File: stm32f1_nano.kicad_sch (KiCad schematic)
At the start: 49 parts, among them J1 Analog, J2 Digital, J3 TYPE-C-31-M-12, J5 DEBUG, Q1 AO3401A, U1 STM32F103C8T6, U2 W25Q128JVSIQ, U3 AMS1117-3.3, U4 XC6206P332MR, U5 AMS1117-5.0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

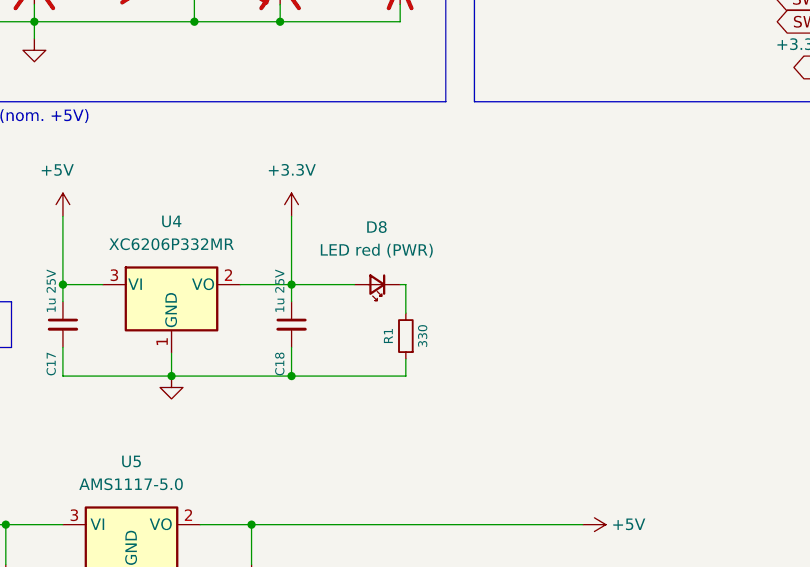
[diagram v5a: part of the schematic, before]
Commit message: #8 Use green power led
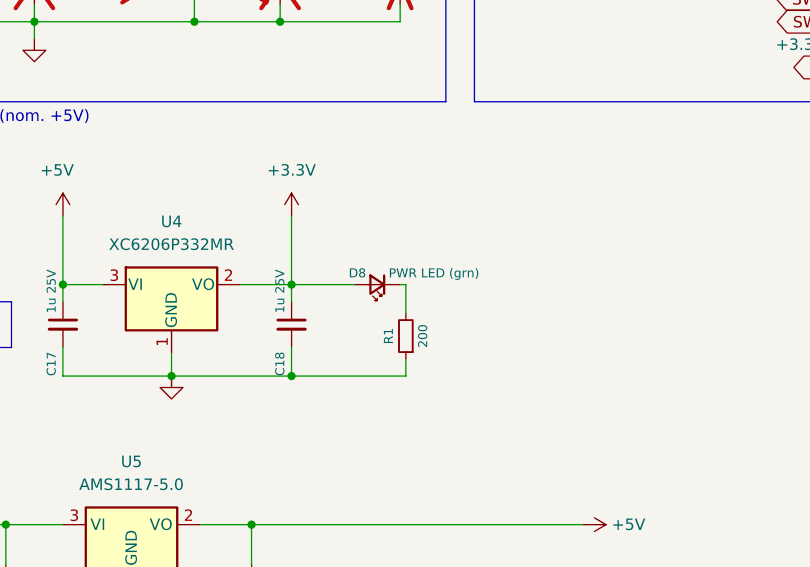
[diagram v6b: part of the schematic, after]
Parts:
- D8: value LED red (PWR) -> PWR LED (grn); JLCPCB Part # C2286 -> C72043; Manufacturer Hubei KENTO Elec -> Everlight Elec; Manufacturer_Name Hubei KENTO Elec -> Everlight Elec; Manufacturer_Part_Number KT-0603R -> 19-217/GHC-YR1S2/3T; Partnumber KT-0603R -> 19-217/GHC-YR1S2/3T
- R1: value 330 -> 200; JLCPCB Part # C25104 -> C25087; Partnumber 0402WGF3300TCE -> 0402WGF2000TCE
- U4: footprint Package_TO_SOT_SMD:SOT-23-3 -> Package_TO_SOT_SMD:SOT-23
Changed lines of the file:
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@@
     )
   )
-  (symbol (lib_id "Device:R_Small") (at 82.55 153.035 180) (unit 1)
-    (in_bom yes) (on_board yes) (dnp no)
-    (property "Reference" "R1" (at 80.645 153.035 90)
-      (effects (font (size 1 1)))
-    )
-    (property "Value" "330" (at 84.455 153.035 90)
-      (effects (font (size 1 1)))
-    )
-    (property "Footprint" "Resistor_SMD:R_0402_1005Metric" (at 82.55 153.035 0)
-      (effects (font (size 1.27 1.27)) hide)
-    )
-    (property "Datasheet" "~" (at 82.55 153.035 0)
-      (effects (font (size 1.27 1.27)) hide)
-    )
-    (property "Description" "62.5mW Thick Film Resistors ±100ppm/℃ ±1% 330Ω 0402  Chip Resistor - Surface Mount ROHS" (at 82.55 153.035 0)
-      (effects (font (size 1.27 1.27)) hide)
-    )
-    (property "JLCPCB Part #" "C25104" (at 82.55 153.035 0)
-      (effects (font (size 1.27 1.27)) hide)
-    )
-    (property "Manufacturer" "UNI-ROYAL(Uniroyal Elec)" (at 82.55 153.035 0)
-      (effects (font (size 1.27 1.27)) hide)
-    )
-    (property "Partnumber" "0402WGF3300TCE" (at 82.55 153.035 0)
-      (effects (font (size 1.27 1.27)) hide)
-    )
-    (property "isBasicPart" "YES" (at 82.55 153.035 0)
-      (effects (font (size 1.27 1.27)) hide)
-    )
-    (pin "1")
-    (pin "2")
-    (instances
-      (project "stm32f1_nano"
-        (path "/0d35483a-0b12-46cc-b9f2-896fd6831779"
-          (reference "R1") (unit 1)
-        )
-      )
-      (project "stm32f407vg"
-        (path "/2d452db2-a0cd-4a57-9497-df1dd0591a30"
-          (reference "R123") (unit 1)
-        )
-        (path "/2d452db2-a0cd-4a57-9497-df1dd0591a30/cb9cd892-4fab-4f54-9695-d8ba54556bb0"
-          (reference "R252") (unit 1)
-        )
-        (path "/2d452db2-a0cd-4a57-9497-df1dd0591a30/480569e0-5dbc-4314-a9d6-1dbd834f5833"
-          (reference "R502") (unit 1)
-        )
-        (path "/2d452db2-a0cd-4a57-9497-df1dd0591a30/3fc0c7b9-3f68-401d-a562-a4bf607ef36a"
-          (reference "R301") (unit 1)
-        )
-      )
-      (project "basicparts"
-        (path "/43a31acf-2604-4bbd-9556-e633c3dff6c4"
-          (reference "R114") (unit 1)
-        )
-      )
-    )
-  )
   (symbol (lib_id "power:+12V") (at 29.845 62.23 90) (unit 1)
     (in_bom yes) (on_board yes) (dnp no)
@@
     )
   )
+  (symbol (lib_id "Device:LED_Small") (at 79.375 147.32 180) (unit 1)
+    (in_bom yes) (on_board yes) (dnp no)
+    (property "Reference" "D8" (at 76.2 146.05 0)
+      (effects (font (size 1 1)) (justify right))
+    )
+    (property "Value" "PWR LED (grn)" (at 80.645 146.05 0)
+      (effects (font (size 1 1)) (justify right))
+    )
+    (property "Footprint" "LED_SMD:LED_0603_1608Metric" (at 79.375 147.32 90)
+      (effects (font (size 1 1)) hide)
+    )
+    (property "Datasheet" "https://datasheet.lcsc.com/lcsc/1811101510_Everlight-Elec-19-217-GHC-YR1S2-3T_C72043.pdf" (at 79.375 147.32 90)
+      (effects (font (size 1 1)) hide)
+    )
+    (property "Description" "Colorless transparence -40℃~+85℃ 520nm~535nm Emerald 120° 110mW 0603  Light Emitting Diodes (LED) ROHS" (at 79.375 147.32 0)
+      (effects (font (size 1 1)) hide)
+    )
+    (property "Manufacturer" "Everlight Elec" (at 79.375 147.32 0)
+      (effects (font (size 1 1)) hide)
+    )
+    (property "Partnumber" "19-217/GHC-YR1S2/3T" (at 79.375 147.32 0)
+      (effects (font (size 1 1)) hide)
+    )
+    (property "JLCPCB Part #" "C72043" (at 79.375 147.32 0)
+      (effects (font (size 1 1)) hide)
+    )
+    (property "Manufacturer_Name" "Everlight Elec" (at 79.375 147.32 0)
+      (effects (font (size 1 1)) hide)
+    )
+    (property "Manufacturer_Part_Number" "19-217/GHC-YR1S2/3T" (at 79.375 147.32 0)
+      (effects (font (size 1 1)) hide)
+    )
+    (property "isBasicPart" "YES" (at 79.375 147.32 0)
+      (effects (font (size 1 1)) hide)
+    )
+    (pin "1")
+    (pin "2")
+    (instances
+      (project "stm32f1_nano"
+        (path "/0d35483a-0b12-46cc-b9f2-896fd6831779"
+          (reference "D8") (unit 1)
+        )
+      )
+      (project "stm32f407vg"
+        (path "/2d452db2-a0cd-4a57-9497-df1dd0591a30"
+          (reference "D1") (unit 1)
+        )
+        (path "/2d452db2-a0cd-4a57-9497-df1dd0591a30/3fc0c7b9-3f68-401d-a562-a4bf607ef36a"
+          (reference "D301") (unit 1)
+        )
+      )
+      (project "basicparts"
+        (path "/43a31acf-2604-4bbd-9556-e633c3dff6c4"
+          (reference "D3") (unit 1)
+        )
+      )
+    )
+  )
   (symbol (lib_id "Regulator_Linear:AMS1117-3.3") (at 59.055 107.95 0) (unit 1)
     (in_bom no) (on_board no) (dnp yes) (fields_autoplaced)
@@
       (effects (font (size 1.27 1.27)))
     )
-    (property "Footprint" "Package_TO_SOT_SMD:SOT-23-3" (at 56.515 141.605 0)
+    (property "Footprint" "Package_TO_SOT_SMD:SOT-23" (at 56.515 141.605 0)
       (effects (font (size 1.27 1.27) italic) hide)
     )
@@
     )
   )
+  (symbol (lib_id "Device:R_Small") (at 82.55 153.035 180) (unit 1)
+    (in_bom yes) (on_board yes) (dnp no)
+    (property "Reference" "R1" (at 80.645 153.035 90)
+      (effects (font (size 1 1)))
+    )
+    (property "Value" "200" (at 84.455 153.035 90)
+      (effects (font (size 1 1)))
+    )
+    (property "Footprint" "Resistor_SMD:R_0402_1005Metric" (at 82.55 153.035 0)
+      (effects (font (size 1 1)) hide)
+    )
+    (property "Datasheet" "~" (at 82.55 153.035 0)
+      (effects (font (size 1 1)) hide)
+    )
+    (property "Description" "62.5mW Thick Film Resistors ±100ppm/℃ ±1% 200Ω 0402  Chip Resistor - Surface Mount ROHS" (at 82.55 153.035 0)
+      (effects (font (size 1 1)) hide)
+    )
+    (property "JLCPCB Part #" "C25087" (at 82.55 153.035 0)
+      (effects (font (size 1 1)) hide)
+    )
+    (property "Manufacturer" "UNI-ROYAL(Uniroyal Elec)" (at 82.55 153.035 0)
+      (effects (font (size 1 1)) hide)
+    )
+    (property "Partnumber" "0402WGF2000TCE" (at 82.55 153.035 0)
+      (effects (font (size 1 1)) hide)
+    )
+    (property "isBasicPart" "YES" (at 82.55 153.035 0)
+      (effects (font (size 1 1)) hide)
+    )
+    (pin "1")
+    (pin "2")
+    (instances
+      (project "stm32f1_nano"
+        (path "/0d35483a-0b12-46cc-b9f2-896fd6831779"
+          (reference "R1") (unit 1)
+        )
+      )
+      (project "stm32f407vg"
+        (path "/2d452db2-a0cd-4a57-9497-df1dd0591a30"
+          (reference "R123") (unit 1)
+        )
+        (path "/2d452db2-a0cd-4a57-9497-df1dd0591a30/cb9cd892-4fab-4f54-9695-d8ba54556bb0"
+          (reference "R252") (unit 1)
+        )
+        (path "/2d452db2-a0cd-4a57-9497-df1dd0591a30/480569e0-5dbc-4314-a9d6-1dbd834f5833"
+          (reference "R503") (unit 1)
+        )
+      )
+      (project "basicparts"
+        (path "/43a31acf-2604-4bbd-9556-e633c3dff6c4"
+          (reference "R8") (unit 1)
+        )
+      )
+    )
+  )
   (symbol (lib_id "Device:R_Small") (at 81.915 113.665 180) (unit 1)
     (in_bom no) (on_board no) (dnp yes)
@@
         )
       )
-    )
-  )
-  (symbol (lib_id "Device:LED_Small") (at 79.375 147.32 180) (unit 1)
-    (in_bom yes) (on_board yes) (dnp no) (fields_autoplaced)
-    (property "Reference" "D8" (at 79.3115 140.97 0)
-      (effects (font (size 1.27 1.27)))
-    )
-    (property "Value" "LED red (PWR)" (at 79.3115 143.51 0)
-      (effects (font (size 1.27 1.27)))
-    )
-    (property "Footprint" "LED_SMD:LED_0603_1608Metric" (at 79.375 147.32 90)
-      (effects (font (size 1.27 1.27)) hide)
-    )
-    (property "Datasheet" "~" (at 79.375 147.32 90)
-      (effects (font (size 1.27 1.27)) hide)
-    )
-    (property "Description" "-40℃~+85℃ Red 0603  Light Emitting Diodes (LED) ROHS" (at 79.375 147.32 0)
-      (effects (font (size 1.27 1.27)) hide)
-    )
-    (property "Manufacturer" "Hubei KENTO Elec" (at 79.375 147.32 0)
-      (effects (font (size 1.27 1.27)) hide)
-    )
-    (property "Partnumber" "KT-0603R" (at 79.375 147.32 0)
-      (effects (font (size 1.27 1.27)) hide)
-    )
-    (property "JLCPCB Part #" "C2286" (at 79.375 147.32 0)
-      (effects (font (size 1.27 1.27)) hide)
-    )
-    (property "Manufacturer_Name" "Hubei KENTO Elec" (at 79.375 147.32 0)
-      (effects (font (size 1.27 1.27)) hide)
-    )
-    (property "Manufacturer_Part_Number" "KT-0603R" (at 79.375 147.32 0)
-      (effects (font (size 1.27 1.27)) hide)
-    )
-    (property "isBasicPart" "YES" (at 79.375 147.32 0)
-      (effects (font (size 1.27 1.27)) hide)
-    )
-    (pin "1")
-    (pin "2")
-    (instances
-      (project "stm32f1_nano"
-        (path "/0d35483a-0b12-46cc-b9f2-896fd6831779"
-          (reference "D8") (unit 1)
-        )
-      )
-      (project "stm32f407vg"
-        (path "/2d452db2-a0cd-4a57-9497-df1dd0591a30"
-          (reference "D1") (unit 1)
-        )
-        (path "/2d452db2-a0cd-4a57-9497-df1dd0591a30/3fc0c7b9-3f68-401d-a562-a4bf607ef36a"
-          (reference "D301") (unit 1)
-        )
-      )
-      (project "basicparts"
-        (path "/43a31acf-2604-4bbd-9556-e633c3dff6c4"
-          (reference "D105") (unit 1)
-        )
-      )

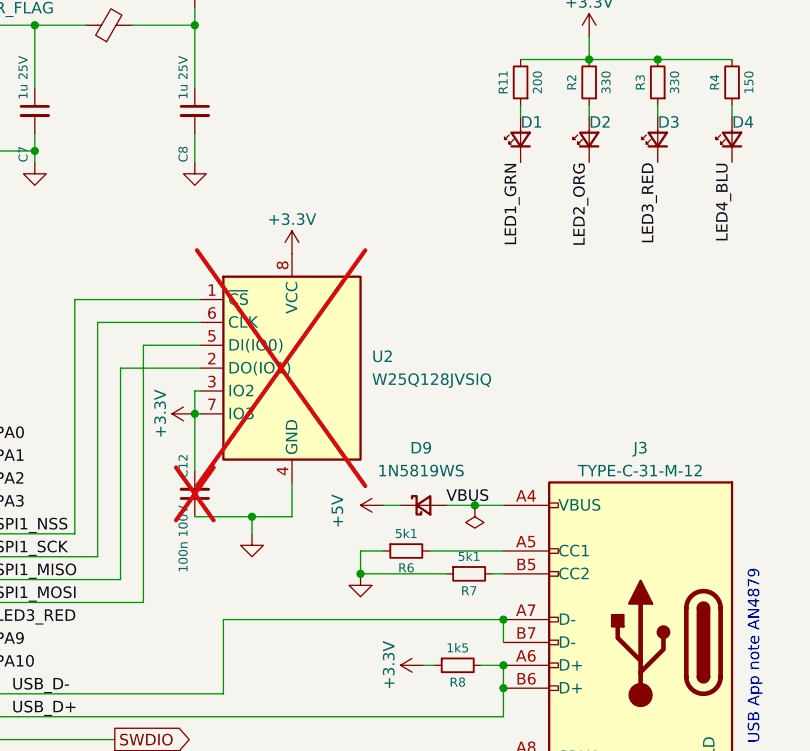
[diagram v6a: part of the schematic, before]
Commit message: #7 Change W25 for a SST26
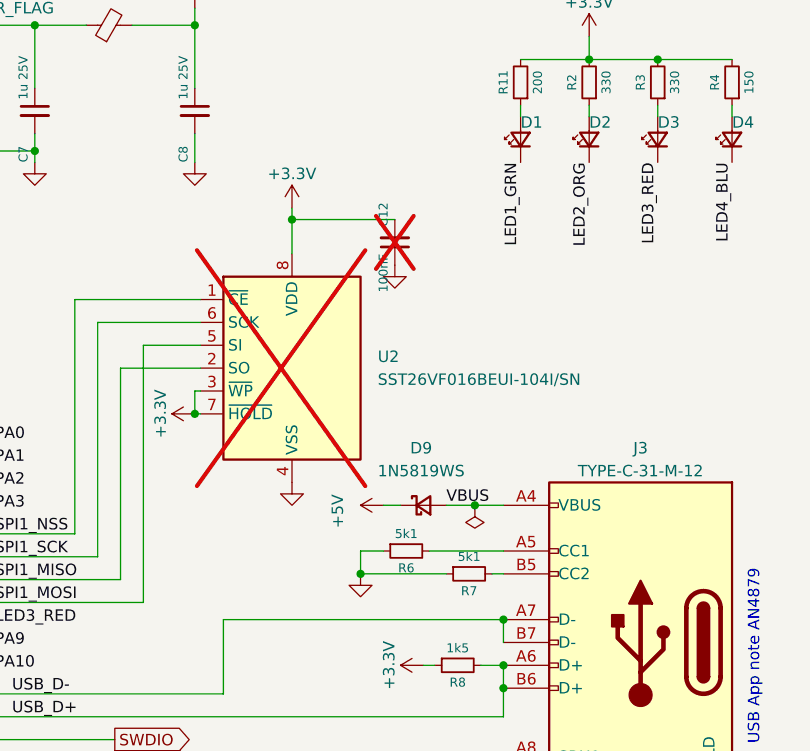
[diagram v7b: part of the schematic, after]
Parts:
- C12: value 100n 100V -> 100nF
- U2: value W25Q128JVSIQ -> SST26VF016BEUI-104I/SN; footprint Package_SO:SOIC-8_5.23x5.23mm_P1.27mm -> Package_SO:SOIC-8_3.9x4.9mm_P1.27mm; symbol Memory_Flash:W25Q32JVSS -> #IC:Microchip Technology SST26VF016BEUI-104I/SN; JLCPCB Part # (none) -> C631791; Manufacturer (none) -> Microchip Tech; Partnumber (none) -> SST26VF016BEUI-104I/SN; isBasicPart (none) -> NO; now in the parts list
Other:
- moved on the sheet: C12

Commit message: Release 1.1.0 sent to JLCPCB
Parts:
- J5: now left out of the parts list
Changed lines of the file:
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@@
     (title "STM32F1 Nano")
     (date "2023-09-05")
-    (rev "1.1.x-dev")
+    (rev "1.1.0")
     (company "easy-smart solution GmbH")
   )
@@
   )
   (symbol (lib_id "Connector_Generic:Conn_01x05") (at 137.16 118.11 0) (unit 1)
-    (in_bom yes) (on_board yes) (dnp no) (fields_autoplaced)
+    (in_bom no) (on_board yes) (dnp no) (fields_autoplaced)
     (property "Reference" "J5" (at 140.335 118.11 0)
       (effects (font (size 1.27 1.27)) (justify left))
